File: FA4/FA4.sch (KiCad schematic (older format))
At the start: 51 parts, among them J1 Cin, J10 COut, J11 S0Out, J12 S1Out, J13 S2Out, J14 S3Out, J15 CinThru, J16 ThruA0, J17 ThruA1, J18 ThruA2, J19 ThruA3, J2 InA0, J20 ThruB0, J21 ThruB1, J22 ThruB2, J23 ThruB3, J3 InA1, J4 InA2, J5 InA3, J6 InB0, J7 InB1, J8 InB2, J9 InB3

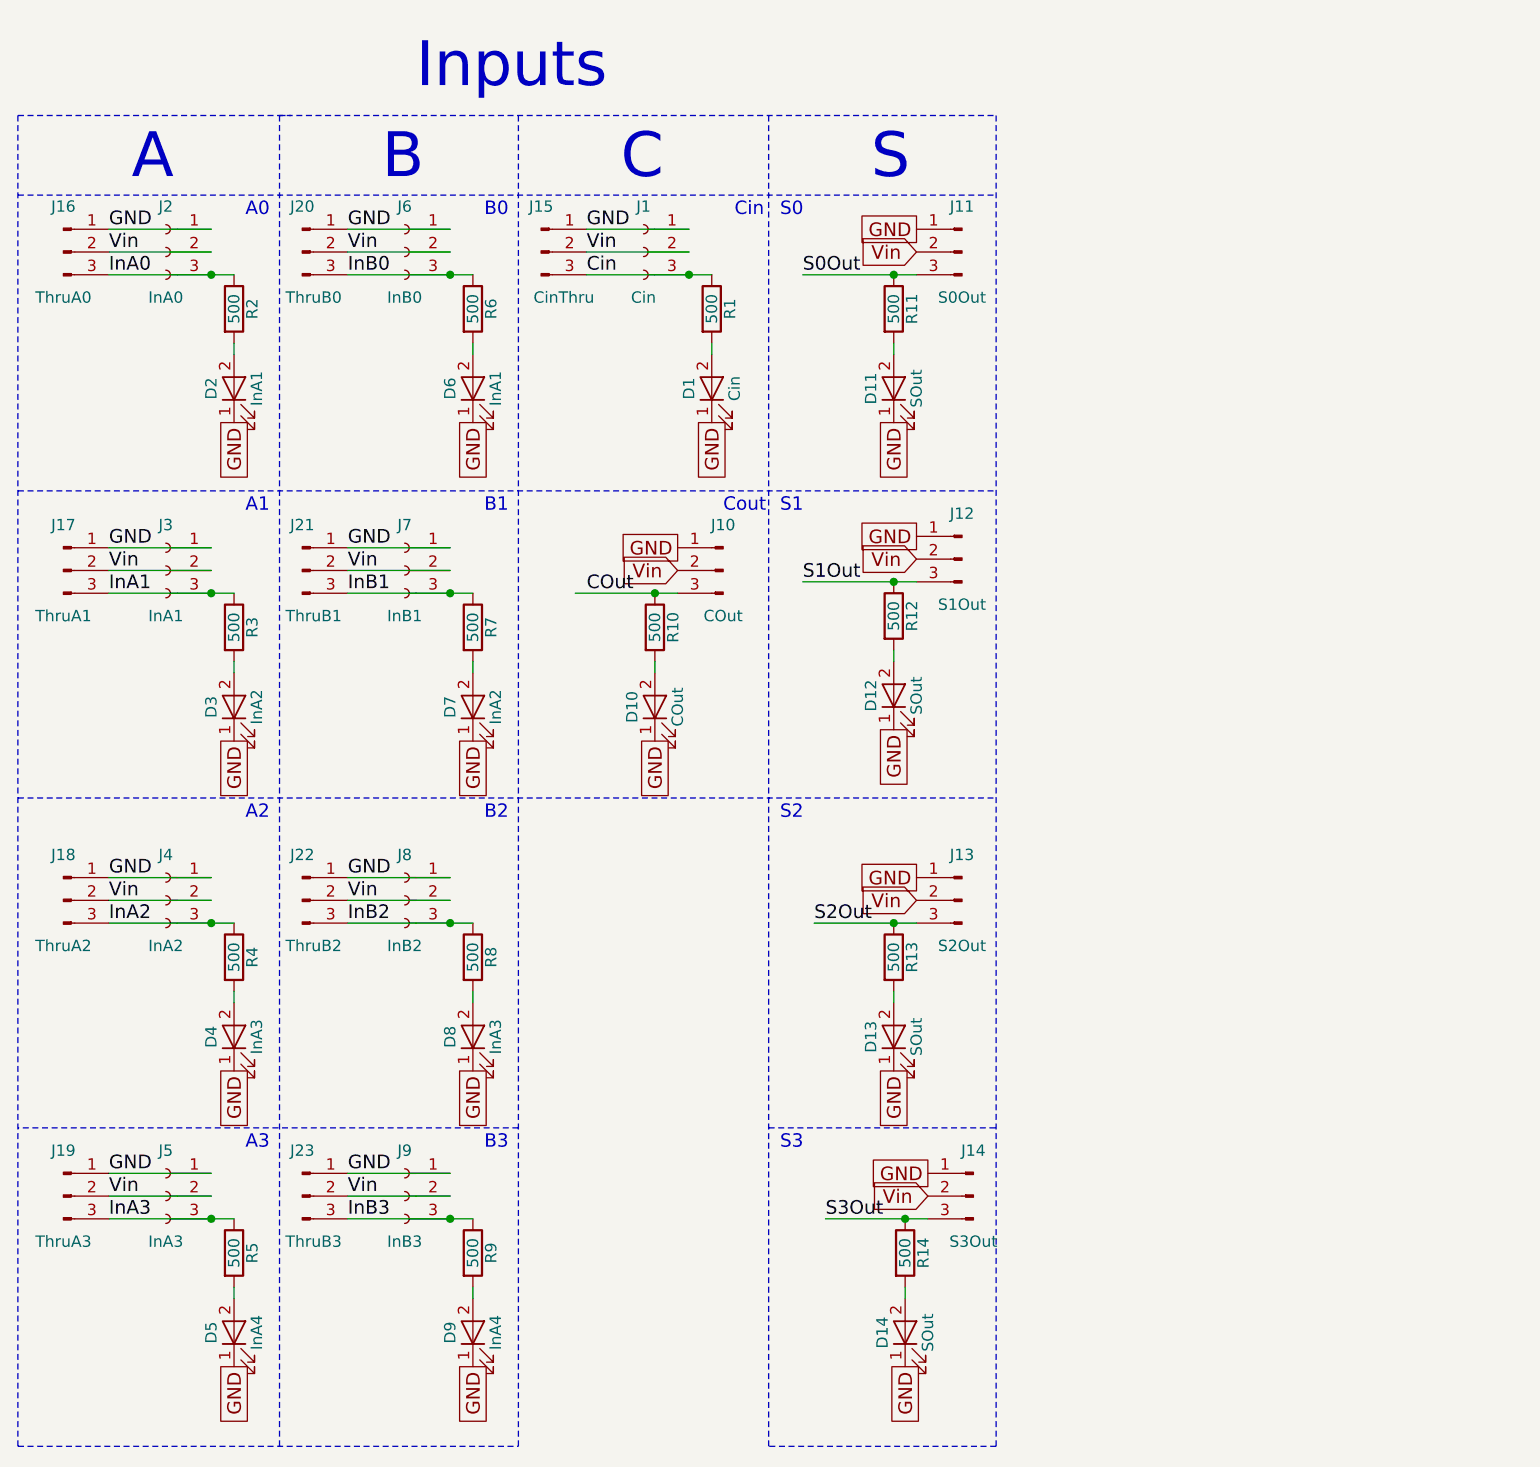
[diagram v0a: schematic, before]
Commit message: Made XOR Board and modified FA
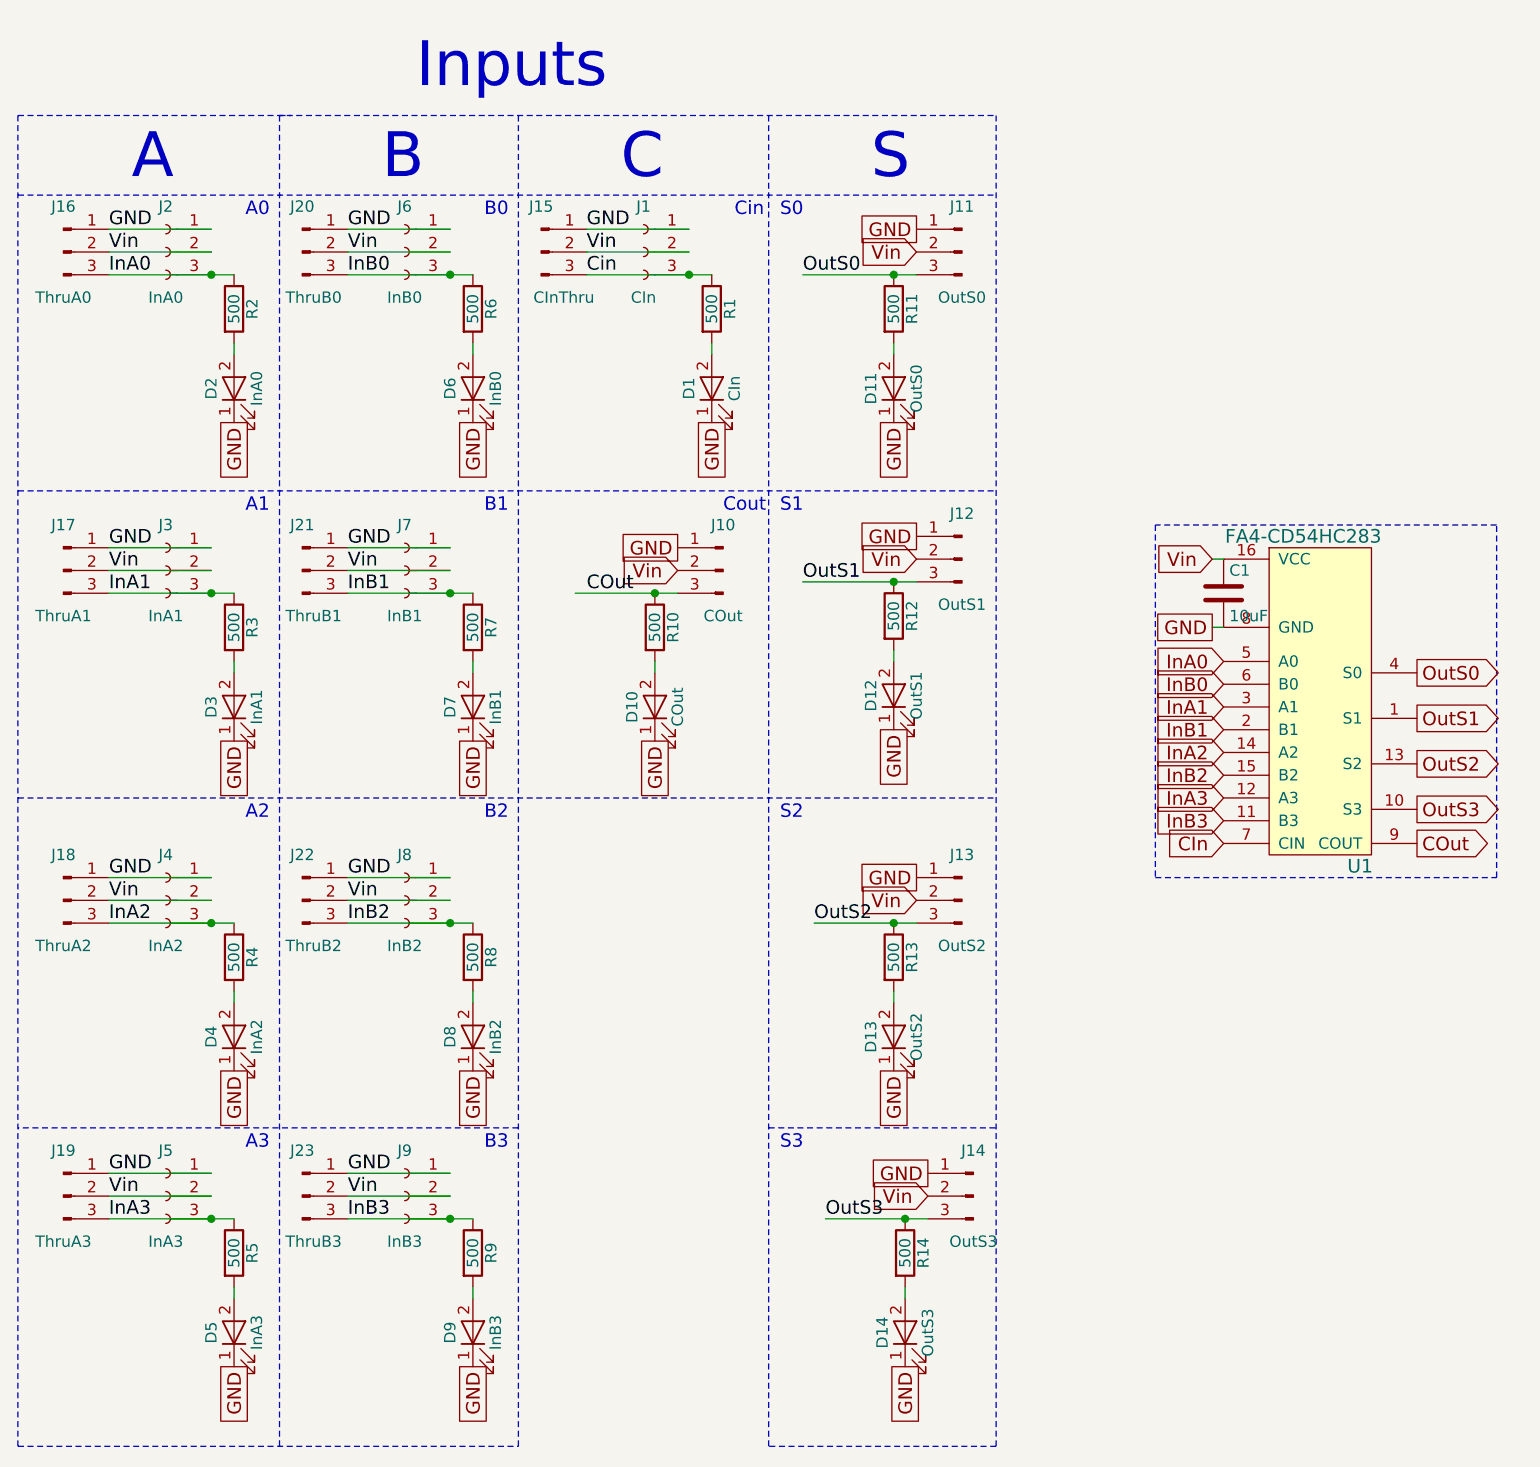
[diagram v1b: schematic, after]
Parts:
- added C1: 10uF, Capacitors_SMD:C_0603_HandSoldering, symbol C
- added U1: FA4-CD54HC283, Housings_SOIC:SOIC-16W_5.3x10.2mm_Pitch1.27mm, symbol FA4-CD54HC283
- D1: value Cin -> CIn; footprint (none) -> LEDs:LED_0603_HandSoldering
- D10: footprint (none) -> LEDs:LED_0603_HandSoldering
- D11: value SOut -> OutS0; footprint (none) -> LEDs:LED_0603_HandSoldering
- D12: value SOut -> OutS1; footprint (none) -> LEDs:LED_0603_HandSoldering
- D13: value SOut -> OutS2; footprint (none) -> LEDs:LED_0603_HandSoldering
- D14: value SOut -> OutS3; footprint (none) -> LEDs:LED_0603_HandSoldering
- D2: value InA1 -> InA0; footprint (none) -> LEDs:LED_0603_HandSoldering
- D3: value InA2 -> InA1; footprint (none) -> LEDs:LED_0603_HandSoldering
- D4: value InA3 -> InA2; footprint (none) -> LEDs:LED_0603_HandSoldering
- D5: value InA4 -> InA3; footprint (none) -> LEDs:LED_0603_HandSoldering
- D6: value InA1 -> InB0; footprint (none) -> LEDs:LED_0603_HandSoldering
- D7: value InA2 -> InB1; footprint (none) -> LEDs:LED_0603_HandSoldering
- D8: value InA3 -> InB2; footprint (none) -> LEDs:LED_0603_HandSoldering
- D9: value InA4 -> InB3; footprint (none) -> LEDs:LED_0603_HandSoldering
- J1: value Cin -> CIn; footprint (none) -> Socket_Strips:Socket_Strip_Angled_1x03_Pitch2.54mm
- J10, J16, J17, J18, J19, J20, J21, J22, J23: footprint (none) -> Pin_Headers:Pin_Header_Angled_1x03_Pitch2.54mm
- J11: value S0Out -> OutS0; footprint (none) -> Pin_Headers:Pin_Header_Angled_1x03_Pitch2.54mm
- J12: value S1Out -> OutS1; footprint (none) -> Pin_Headers:Pin_Header_Angled_1x03_Pitch2.54mm
- J13: value S2Out -> OutS2; footprint (none) -> Pin_Headers:Pin_Header_Angled_1x03_Pitch2.54mm
- J14: value S3Out -> OutS3; footprint (none) -> Pin_Headers:Pin_Header_Angled_1x03_Pitch2.54mm
- J15: value CinThru -> CInThru; footprint (none) -> Pin_Headers:Pin_Header_Angled_1x03_Pitch2.54mm
- J2, J3, J4, J5, J6, J7, J8, J9: footprint (none) -> Socket_Strips:Socket_Strip_Angled_1x03_Pitch2.54mm
- R1, R10, R11, R12, R13, R14, R2, R3, R4, R5, R6, R7, R8, R9: footprint (none) -> Resistors_SMD:R_0603_HandSoldering
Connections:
- net COut: now also U1.9 (COUT)
- net GND: now also C1.2, U1.8 (GND)
- net InA0: now also U1.5 (A0)
- net InA1: now also U1.3 (A1)
- net InA2: now also U1.14 (A2)
- net InA3: now also U1.12 (A3)
- net InB0: now also U1.6 (B0)
- net InB1: now also U1.2 (B1)
- net InB2: now also U1.15 (B2)
- net InB3: now also U1.11 (B3)
- net Vin: now also C1.1, U1.16 (VCC)
- net S0Out renamed OutS0
- net OutS0: now also U1.4 (S0)
- net S1Out renamed OutS1
- net OutS1: now also U1.1 (S1)
- net S2Out renamed OutS2
- net OutS2: now also U1.13 (S2)
- net S3Out renamed OutS3
- net OutS3: now also U1.10 (S3)
- new net CIn: U1.7 (CIN)
